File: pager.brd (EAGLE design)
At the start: 78.4 x 44.8 mm, 62 parts, among them Q1 25 MHz, Q2 SI2333DS, SW1 CHS-01A1, SW2 CHS-01A1, U1 VOCORE2-SMD, U2 VOCORE2-SMD, U3 XR22800IL, X1 OMRON_XF2L-30REVERSE, X2 FCI_8193_MICRO_USB

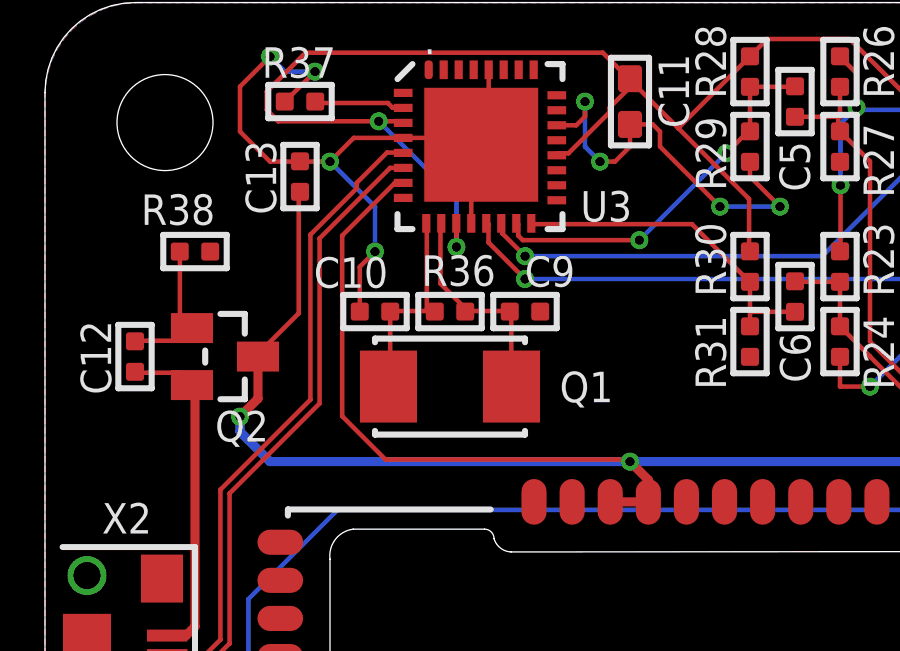
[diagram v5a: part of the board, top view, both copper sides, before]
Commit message: 5V to USB chip nicer
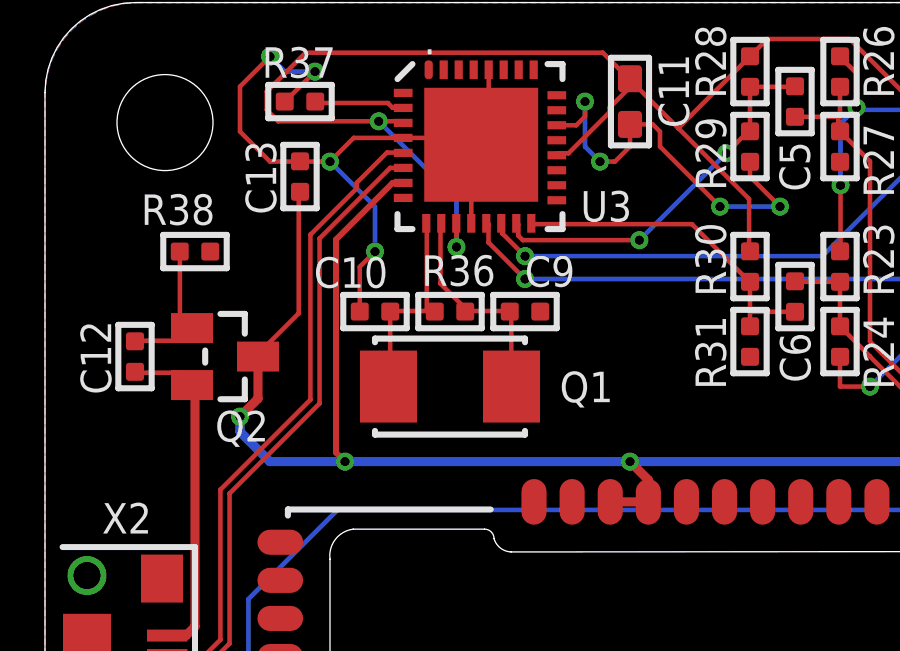
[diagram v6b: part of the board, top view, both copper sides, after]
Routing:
- net +5V: track 112.6 -> 104.3 mm, vias 4 -> 5
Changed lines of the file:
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@@
 <wire x1="6.5" y1="31" x2="6.5" y2="30.5" width="0.3048" layer="16"/>
 <wire x1="6.5" y1="30.5" x2="7.5" y2="29.5" width="0.3048" layer="16"/>
-<wire x1="7.5" y1="29.5" x2="19.5" y2="29.5" width="0.3048" layer="16"/>
+<wire x1="7.5" y1="29.5" x2="10" y2="29.5" width="0.3048" layer="16"/>
+<wire x1="10" y1="29.5" x2="19.5" y2="29.5" width="0.3048" layer="16"/>
 <wire x1="19.5" y1="29.5" x2="37" y2="29.5" width="0.3048" layer="16"/>
 <wire x1="37" y1="29.5" x2="38.5" y2="28" width="0.3048" layer="16"/>
@@
 <wire x1="8.4582" y1="38.481" x2="8.5" y2="38.492" width="0.1524" layer="1"/>
 <wire x1="7.1628" y1="33.147" x2="7.1" y2="33" width="0.1524" layer="1"/>
-<wire x1="11.6586" y1="38.7858" x2="11.8872" y2="38.7858" width="0.1524" layer="1"/>
-<wire x1="9.906" y1="37.0332" x2="11.6586" y2="38.7858" width="0.1524" layer="1"/>
-<wire x1="9.906" y1="31.0134" x2="9.906" y2="37.0332" width="0.1524" layer="1"/>
-<wire x1="11.3538" y1="29.5656" x2="9.906" y2="31.0134" width="0.1524" layer="1"/>
-<wire x1="19.3548" y1="29.5656" x2="11.3538" y2="29.5656" width="0.1524" layer="1"/>
 <wire x1="11.8872" y1="38.7858" x2="11.94" y2="38.79" width="0.1524" layer="1"/>
 <wire x1="19.3548" y1="29.5656" x2="19.5" y2="29.5" width="0.1524" layer="1"/>
+<wire x1="11.8872" y1="38.7858" x2="11.5858" y2="38.7858" width="0.2" layer="1"/>
+<wire x1="11.5858" y1="38.7858" x2="9.7" y2="36.9" width="0.2" layer="1"/>
+<wire x1="9.7" y1="36.9" x2="9.7" y2="29.8" width="0.2" layer="1"/>
+<wire x1="9.7" y1="29.8" x2="10" y2="29.5" width="0.2" layer="1"/>
+<via x="10" y="29.5" extent="1-16" drill="0.3048"/>
 </signal>
 <signal name="GND" class="3">

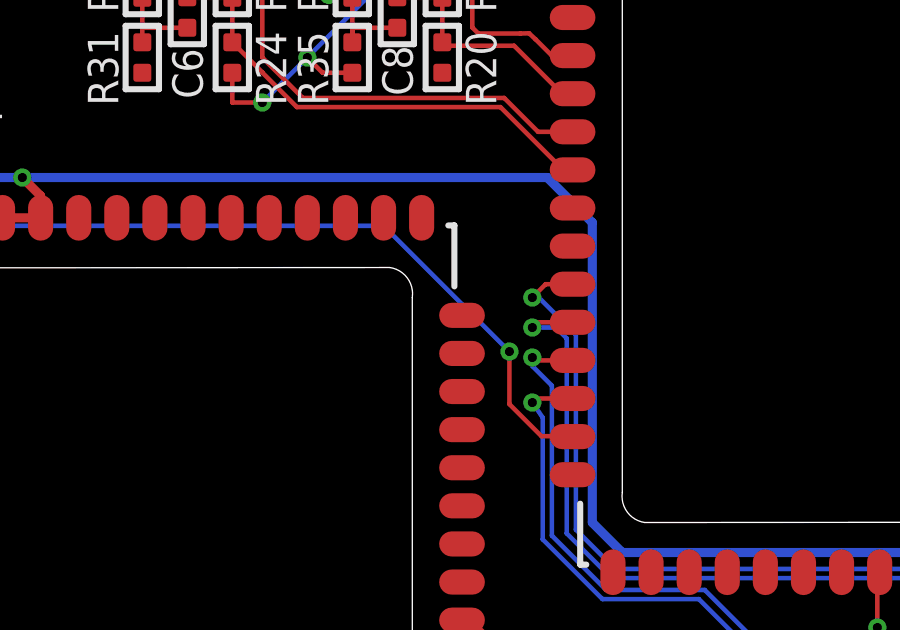
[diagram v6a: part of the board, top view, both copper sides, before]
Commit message: moved wire to make ground-plane continue better between U1 and U2
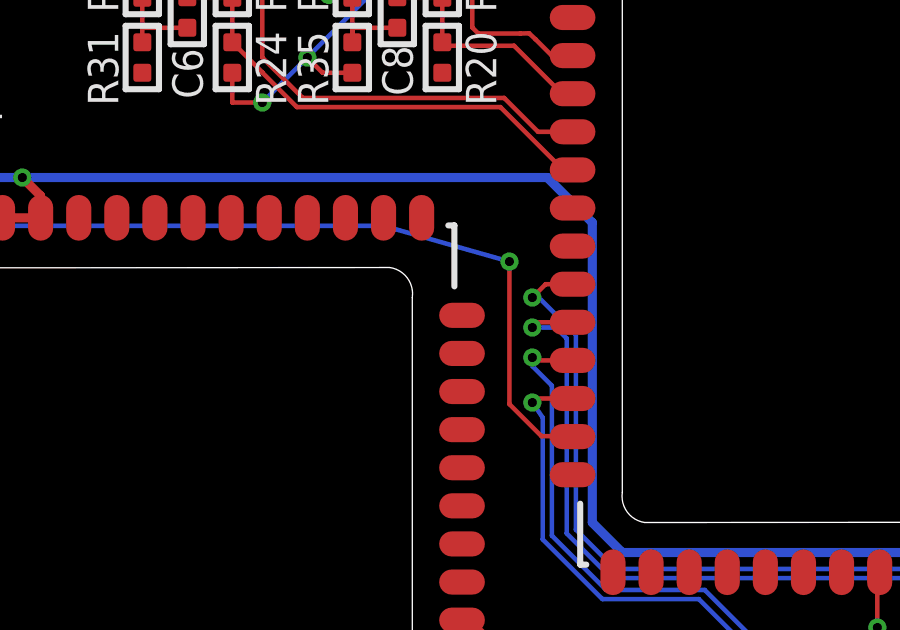
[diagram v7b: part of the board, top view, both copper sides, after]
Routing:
- net WIFI_RESET: track 42.4 -> 43.9 mm
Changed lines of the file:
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@@
 <wire x1="9.7536" y1="27.8892" x2="6.7818" y2="24.9174" width="0.1524" layer="16"/>
 <wire x1="31.5468" y1="27.8892" x2="9.7536" y2="27.8892" width="0.1524" layer="16"/>
-<wire x1="35.7378" y1="23.6982" x2="31.5468" y2="27.8892" width="0.1524" layer="16"/>
-<wire x1="35.7378" y1="21.9456" x2="35.7378" y2="23.6982" width="0.1524" layer="1"/>
+<wire x1="35.7378" y1="26.6982" x2="31.5468" y2="27.8892" width="0.1524" layer="16"/>
+<wire x1="35.7378" y1="21.9456" x2="35.7378" y2="26.6982" width="0.1524" layer="1"/>
 <wire x1="36.8046" y1="20.8788" x2="35.7378" y2="21.9456" width="0.1524" layer="1"/>
 <wire x1="37.7952" y1="20.8788" x2="36.8046" y2="20.8788" width="0.1524" layer="1"/>
@@
 <wire x1="37.7952" y1="20.8788" x2="37.8428" y2="20.864" width="0.1524" layer="1"/>
 <via x="6.7818" y="22.479" extent="1-16" drill="0.3048"/>
-<via x="35.7378" y="23.6982" extent="1-16" drill="0.3048"/>
+<via x="35.7378" y="26.6982" extent="1-16" drill="0.3048"/>
 </signal>
 </signals>

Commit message: Newer board file, laforge's tips mostly incorporated
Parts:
- moved TP2 0.50 mm to (59.5, 14.0)
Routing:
- net 3.3_CORE: track 60.7 -> 83.1 mm, vias 7 -> 6
- net 3.3_WIFI: track 54.9 -> 40.7 mm
- net ETH_2B_TX_P: track 22.8 -> 36.3 mm
- net GND: track 71.6 -> 63.4 mm, vias 13 -> 67
- net ETH_2B_TX_N: track 30.1 -> 38.1 mm, vias 2 -> 0
- net ETH_2A_TX_N: track 22.5 -> 30.3 mm
- net 3.3_USB: track 53.3 -> 46.5 mm, vias 2 -> 5
- net ETH_1A_TX_N: track 16.1 -> 21.0 mm
- net ETH_1A_RX_N: track 8.04 -> 12.8 mm
- net ETH_2A_RX_P: track 32.6 -> 36.8 mm
- net WIFI_RESET: track 43.9 -> 47.5 mm
- net ETH_2B_RX_N: track 13.3 -> 16.1 mm
- net ETH_2B_RX_P: track 18.4 -> 15.7 mm
- net ETH_1B_TX_N: track 20.4 -> 23.1 mm
- net +5V: track 104.3 -> 106.6 mm, vias 5 -> 14
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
